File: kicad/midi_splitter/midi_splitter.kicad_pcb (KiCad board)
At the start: 2 copper layers, 96 x 50 mm, 42 parts, among them J1 DIN-5_180degree, J10 DIN-5_180degree, J2 DIN-5_180degree, J3 DIN-5_180degree, J4 DIN-5_180degree, J5 DIN-5_180degree, J7 DIN-5_180degree, J8 DS1099, U1 6N138, U2 MM74HC540MTCX

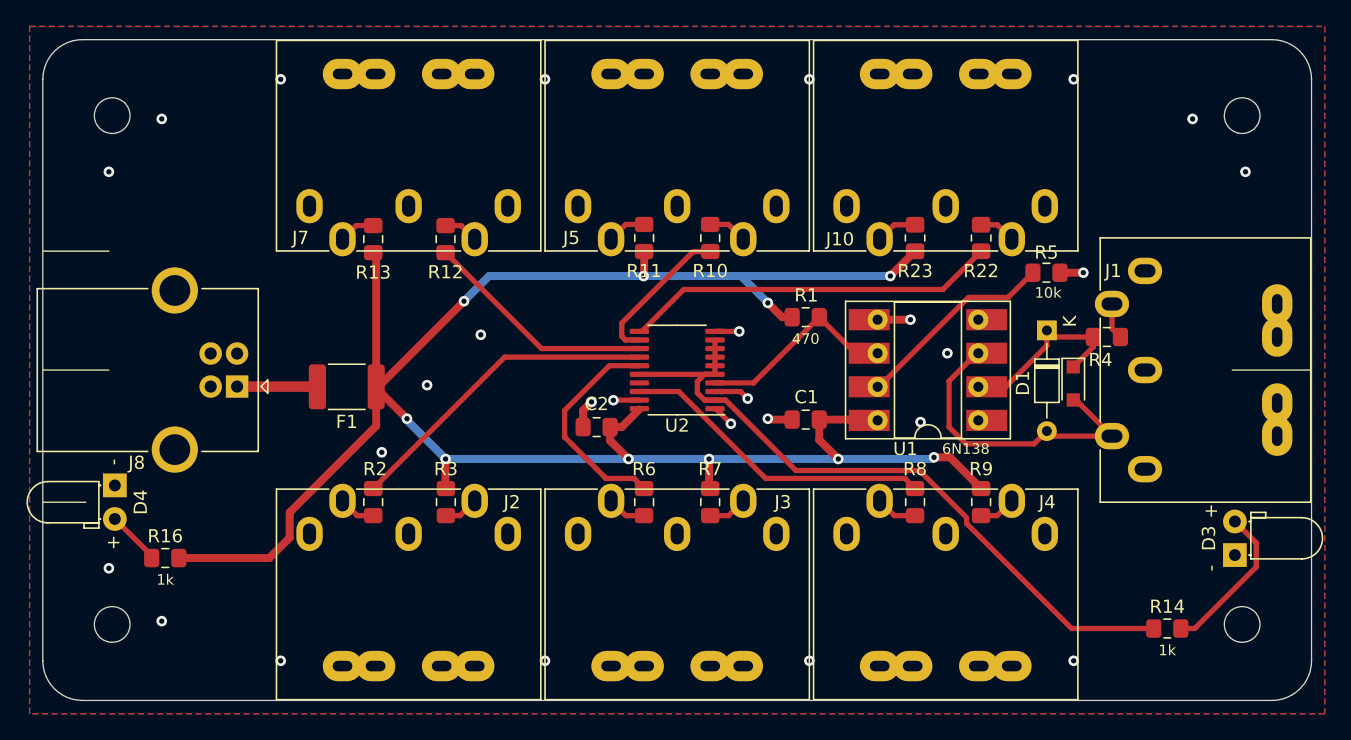
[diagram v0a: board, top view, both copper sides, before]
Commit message: Upgrading to KiCAD 7
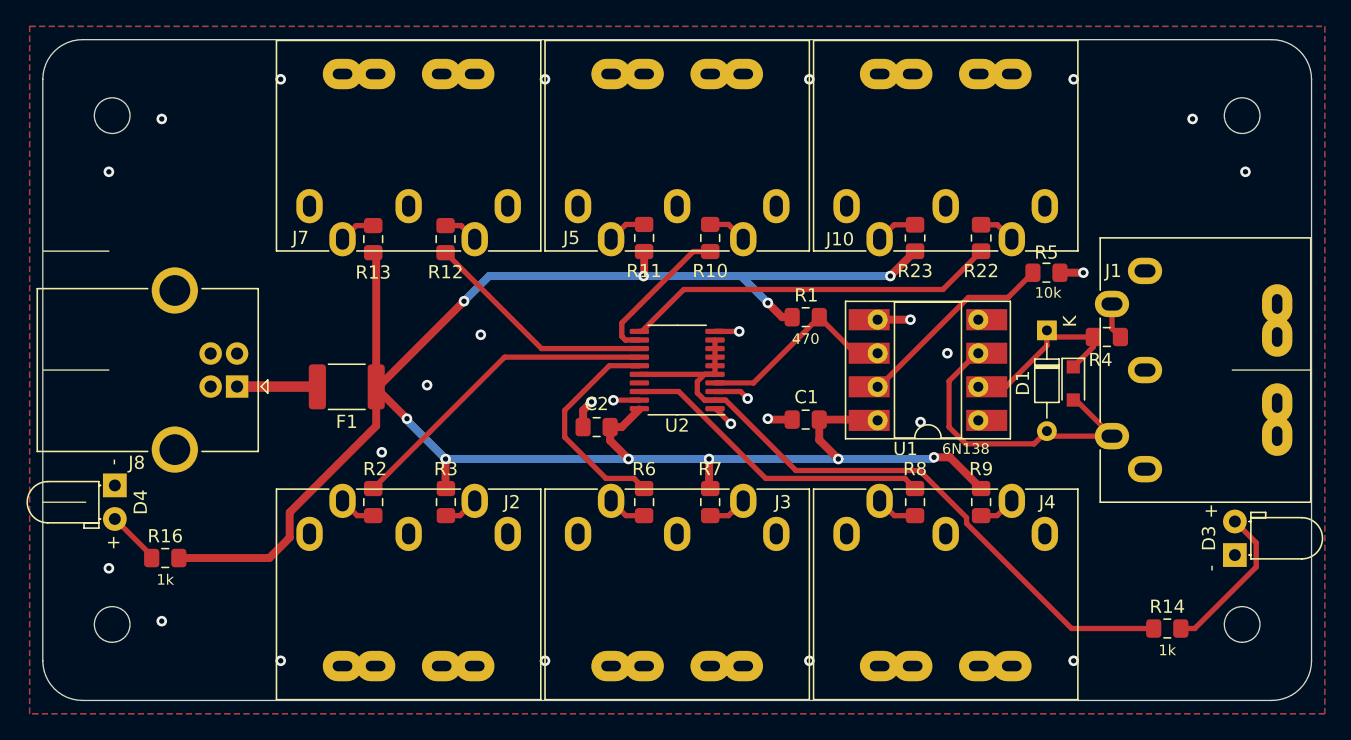
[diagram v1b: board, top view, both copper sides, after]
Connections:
- net ~RX renamed ~{RX}
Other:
- net class Default removed
- net class Thick removed
